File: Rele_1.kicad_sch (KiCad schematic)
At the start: 6 parts, among them J14 Rele_1, J31 Pin GND, K3 SRD-05VDC-SL-C, Q11 PMBT3904,235

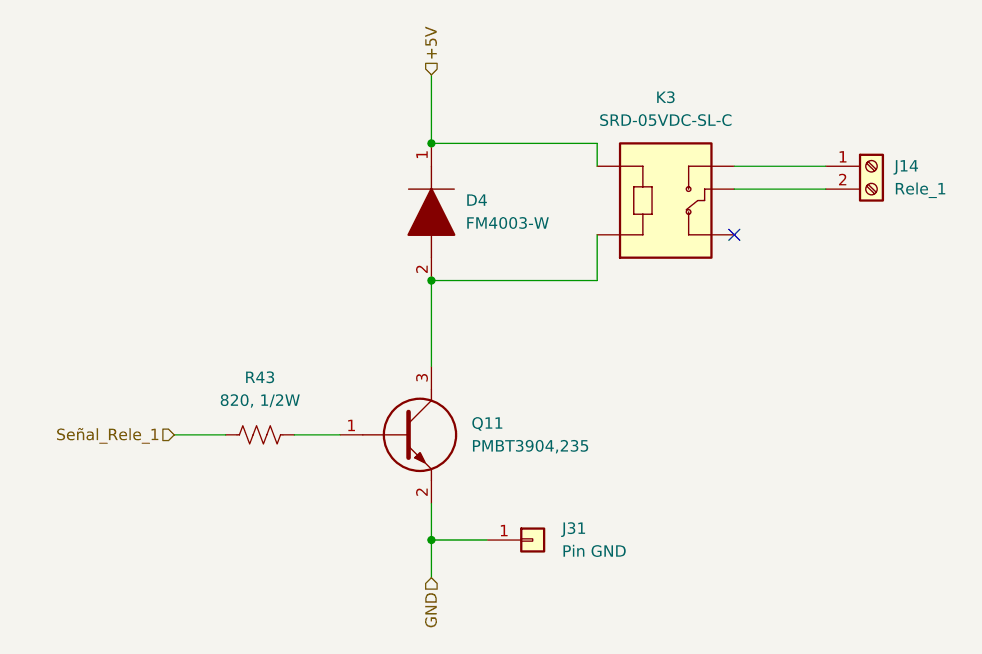
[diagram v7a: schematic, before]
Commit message: Se modificaron algunos componentes, según disponibilidad
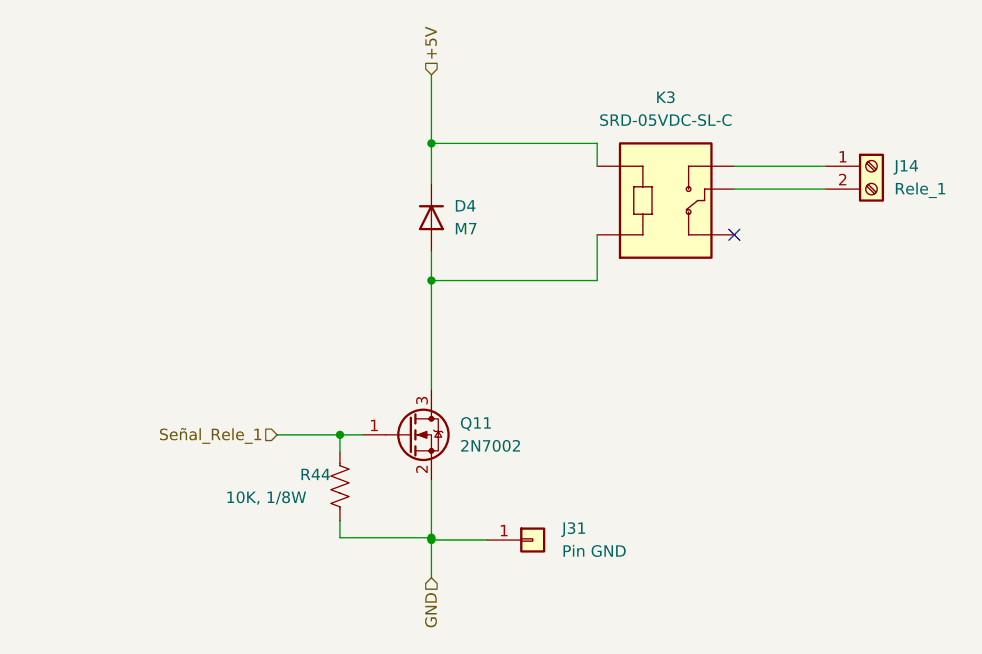
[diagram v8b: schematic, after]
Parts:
- removed D4: FM4003-W, FM4003W:DIOM5025X231N, symbol FM4003-W:FM4003-W
- removed Q11: PMBT3904,235, PMBT3904,235:SOT95P230X110-3N, symbol PMBT3904,235:PMBT3904,235
- removed R43: 820, 1/2W, Resistor_SMD:R_0805_2012Metric, symbol Device:R_US
- added D4: M7, Diode_SMD:D_SMA, symbol Device:D
- added Q11: 2N7002, Package_TO_SOT_SMD:SOT-23, symbol Transistor_FET:2N7002
- added R44: 10K, 1/8W, Resistor_SMD:R_0805_2012Metric, symbol Device:R_US
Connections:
- net +5V: now also D4.1 (K)
- net GND: now also Q11.2 (S), R44.2
- net Señal_Rele_1: now also Q11.1 (G), R44.1
- net at K3.A2: now also D4.2 (A), Q11.3 (D)
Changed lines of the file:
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@@
   (junction (at 139.7 85.09) (diameter 0) (color 0 0 0 0)
+  )
+  (junction (at 129.54 102.235) (diameter 0) (color 0 0 0 0)
+  )
+  (junction (at 139.7 113.665) (diameter 0) (color 0 0 0 0)
+  )
+  (junction (at 139.7 69.85) (diameter 0) (color 0 0 0 0)
   )
   (junction (at 139.7 113.919) (diameter 0) (color 0 0 0 0)
   )
-  (junction (at 139.7 69.85) (diameter 0) (color 0 0 0 0)
-  )
   (no_connect (at 173.355 80.01))
-  (wire (pts (xy 139.7 85.09) (xy 139.7 94.615))
+  (wire (pts (xy 139.7 85.09) (xy 139.7 97.155))
     (stroke (width 0) (type default) (color 0 0 0 0))
   )
@@
     (stroke (width 0) (type default) (color 0 0 0 0))
   )
+  (wire (pts (xy 129.54 113.665) (xy 139.7 113.665))
+    (stroke (width 0) (type default) (color 0 0 0 0))
+  )
   (wire (pts (xy 139.7 113.919) (xy 145.8722 113.919))
     (stroke (width 0) (type default) (color 0 0 0 0))
   )
-  (wire (pts (xy 124.46 102.235) (xy 129.54 102.235))
+  (wire (pts (xy 122.555 102.235) (xy 129.54 102.235))
     (stroke (width 0) (type default) (color 0 0 0 0))
   )
-  (wire (pts (xy 111.125 102.235) (xy 116.84 102.235))
+  (wire (pts (xy 129.54 111.76) (xy 129.54 113.665))
+    (stroke (width 0) (type default) (color 0 0 0 0))
+  )
+  (wire (pts (xy 139.7 69.85) (xy 139.7 74.295))
     (stroke (width 0) (type default) (color 0 0 0 0))
   )
   (wire (pts (xy 158.115 85.09) (xy 158.115 80.01))
+    (stroke (width 0) (type default) (color 0 0 0 0))
+  )
+  (wire (pts (xy 129.54 102.235) (xy 129.54 104.14))
+    (stroke (width 0) (type default) (color 0 0 0 0))
+  )
+  (wire (pts (xy 129.54 102.235) (xy 132.08 102.235))
     (stroke (width 0) (type default) (color 0 0 0 0))
   )
@@
     (stroke (width 0) (type default) (color 0 0 0 0))
   )
-  (wire (pts (xy 139.7 109.855) (xy 139.7 113.919))
+  (wire (pts (xy 139.7 113.665) (xy 139.7 113.919))
+    (stroke (width 0) (type default) (color 0 0 0 0))
+  )
+  (wire (pts (xy 139.7 107.315) (xy 139.7 113.665))
+    (stroke (width 0) (type default) (color 0 0 0 0))
+  )
+  (wire (pts (xy 139.7 81.915) (xy 139.7 85.09))
     (stroke (width 0) (type default) (color 0 0 0 0))
   )
@@
     (stroke (width 0) (type default) (color 0 0 0 0))
   )
-  (hierarchical_label "Señal_Rele_1" (shape input) (at 111.125 102.235 180)
+  (hierarchical_label "Señal_Rele_1" (shape input) (at 122.555 102.235 180)
     (effects (font (size 1.27 1.27)) (justify right))
   )
@@
     (effects (font (size 1.27 1.27)) (justify left))
   )
-  (symbol (lib_id "FM4003-W:FM4003-W") (at 139.7 69.85 270) (unit 1)
+  (symbol (lib_id "Device:D") (at 139.7 78.105 270) (unit 1)
     (in_bom yes) (on_board yes) (fields_autoplaced)
-    (property "Reference" "D4" (id 0) (at 143.51 76.1999 90)
+    (property "Reference" "D4" (id 0) (at 142.24 76.8349 90)
       (effects (font (size 1.27 1.27)) (justify left))
     )
-    (property "Value" "FM4003-W" (id 1) (at 143.51 78.7399 90)
+    (property "Value" "M7" (id 1) (at 142.24 79.3749 90)
       (effects (font (size 1.27 1.27)) (justify left))
     )
-    (property "Footprint" "FM4003W:DIOM5025X231N" (id 2) (at 139.7 81.28 0)
-      (effects (font (size 1.27 1.27)) (justify left) hide)
+    (property "Footprint" "Diode_SMD:D_SMA" (id 2) (at 139.7 78.105 0)
+      (effects (font (size 1.27 1.27)) hide)
     )
-    (property "Datasheet" "https://componentsearchengine.com/Datasheets/1/FM4003-W.pdf" (id 3) (at 137.16 81.28 0)
-      (effects (font (size 1.27 1.27)) (justify left) hide)
-    )
-    (property "Description" "Rectifiers 1A 200V GP" (id 4) (at 134.62 81.28 0)
-      (effects (font (size 1.27 1.27)) (justify left) hide)
-    )
-    (property "Height" "2.31" (id 5) (at 132.08 81.28 0)
-      (effects (font (size 1.27 1.27)) (justify left) hide)
-    )
-    (property "Manufacturer_Name" "Rectron" (id 6) (at 129.54 81.28 0)
-      (effects (font (size 1.27 1.27)) (justify left) hide)
-    )
-    (property "Manufacturer_Part_Number" "FM4003-W" (id 7) (at 127 81.28 0)
-      (effects (font (size 1.27 1.27)) (justify left) hide)
-    )
-    (property "Mouser Part Number" "583-FM4003-W" (id 8) (at 124.46 81.28 0)
-      (effects (font (size 1.27 1.27)) (justify left) hide)
-    )
-    (property "Mouser Price/Stock" "https://www.mouser.co.uk/ProductDetail/Rectron/FM4003-W/?qs=5h8Q3Z7TNRlJu6QU92Ho0w%3D%3D" (id 9) (at 121.92 81.28 0)
-      (effects (font (size 1.27 1.27)) (justify left) hide)
-    )
-    (property "Arrow Part Number" "FM4003-W" (id 10) (at 119.38 81.28 0)
-      (effects (font (size 1.27 1.27)) (justify left) hide)
-    )
-    (property "Arrow Price/Stock" "https://www.arrow.com/en/products/fm4003-w/rectron" (id 11) (at 116.84 81.28 0)
-      (effects (font (size 1.27 1.27)) (justify left) hide)
-    )
-    (property "Mouser Testing Part Number" "" (id 12) (at 114.3 81.28 0)
-      (effects (font (size 1.27 1.27)) (justify left) hide)
-    )
-    (property "Mouser Testing Price/Stock" "" (id 13) (at 111.76 81.28 0)
-      (effects (font (size 1.27 1.27)) (justify left) hide)
+    (property "Datasheet" "~" (id 3) (at 139.7 78.105 0)
+      (effects (font (size 1.27 1.27)) hide)
     )
     (pin "1")
@@
     )
     (pin "1")
+  )
+  (symbol (lib_id "Device:R_US") (at 129.54 107.95 0) (unit 1)
+    (in_bom yes) (on_board yes)
+    (property "Reference" "R44" (id 0) (at 125.095 106.68 0)
+      (effects (font (size 1.27 1.27)) (justify left))
+    )
+    (property "Value" "10K, 1/8W" (id 1) (at 116.84 109.22 0)
+      (effects (font (size 1.27 1.27)) (justify left))
+    )
+    (property "Footprint" "Resistor_SMD:R_0805_2012Metric" (id 2) (at 130.556 108.204 90)
+      (effects (font (size 1.27 1.27)) hide)
+    )
+    (property "Datasheet" "~" (id 3) (at 129.54 107.95 0)
+      (effects (font (size 1.27 1.27)) hide)
+    )
+    (pin "1")
+    (pin "2")
   )
   (symbol (lib_id "SRD-05VDC-SL-C:SRD-05VDC-SL-C") (at 165.735 74.93 0) (unit 1)
@@
     (pin "2")
   )
-  (symbol (lib_id "PMBT3904,235:PMBT3904,235") (at 129.54 102.235 0) (unit 1)
+  (symbol (lib_id "Transistor_FET:2N7002") (at 137.16 102.235 0) (unit 1)
     (in_bom yes) (on_board yes) (fields_autoplaced)
-    (property "Reference" "Q11" (id 0) (at 144.145 100.9649 0)
+    (property "Reference" "Q11" (id 0) (at 142.875 100.9649 0)
       (effects (font (size 1.27 1.27)) (justify left))
     )
-    (property "Value" "PMBT3904,235" (id 1) (at 144.145 103.5049 0)
+    (property "Value" "2N7002" (id 1) (at 142.875 103.5049 0)
       (effects (font (size 1.27 1.27)) (justify left))
     )
-    (property "Footprint" "PMBT3904,235:SOT95P230X110-3N" (id 2) (at 143.51 106.045 0)
-      (effects (font (size 1.27 1.27)) (justify left) hide)
+    (property "Footprint" "Package_TO_SOT_SMD:SOT-23" (id 2) (at 142.24 104.14 0)
+      (effects (font (size 1.27 1.27) italic) (justify left) hide)
     )
-    (property "Datasheet" "https://assets.nexperia.com/documents/data-sheet/PMBT3904.pdf" (id 3) (at 143.51 108.585 0)
-      (effects (font (size 1.27 1.27)) (justify left) hide)
-    )
-    (property "Description" "PMBT3904 - NPN switching transistor" (id 4) (at 143.51 111.125 0)
-      (effects (font (size 1.27 1.27)) (justify left) hide)
-    )
-    (property "Height" "1.1" (id 5) (at 143.51 113.665 0)
-      (effects (font (size 1.27 1.27)) (justify left) hide)
-    )
-    (property "Manufacturer_Name" "Nexperia" (id 6) (at 143.51 116.205 0)
-      (effects (font (size 1.27 1.27)) (justify left) hide)
-    )
-    (property "Manufacturer_Part_Number" "PMBT3904,235" (id 7) (at 143.51 118.745 0)
-      (effects (font (size 1.27 1.27)) (justify left) hide)
-    )
-    (property "Mouser Part Number" "771-PMBT3904235" (id 8) (at 143.51 121.285 0)
-      (effects (font (size 1.27 1.27)) (justify left) hide)
-    )
-    (property "Mouser Price/Stock" "https://www.mouser.co.uk/ProductDetail/Nexperia/PMBT3904235?qs=LOCUfHb8d9uziIfl4fmvZg%3D%3D" (id 9) (at 143.51 123.825 0)
-      (effects (font (size 1.27 1.27)) (justify left) hide)
-    )
-    (property "Arrow Part Number" "PMBT3904,235" (id 10) (at 143.51 126.365 0)
-      (effects (font (size 1.27 1.27)) (justify left) hide)
-    )
-    (property "Arrow Price/Stock" "https://www.arrow.com/en/products/pmbt3904235/nexperia?region=nac" (id 11) (at 143.51 128.905 0)
-      (effects (font (size 1.27 1.27)) (justify left) hide)
-    )
-    (property "Mouser Testing Part Number" "" (id 12) (at 143.51 131.445 0)
-      (effects (font (size 1.27 1.27)) (justify left) hide)
-    )
-    (property "Mouser Testing Price/Stock" "" (id 13) (at 143.51 133.985 0)
+    (property "Datasheet" "https://www.onsemi.com/pub/Collateral/NDS7002A-D.PDF" (id 3) (at 137.16 102.235 0)
       (effects (font (size 1.27 1.27)) (justify left) hide)
     )
@@
     (pin "3")
   )
-  (symbol (lib_id "Device:R_US") (at 120.65 102.235 90) (unit 1)
-    (in_bom yes) (on_board yes) (fields_autoplaced)
-    (property "Reference" "R43" (id 0) (at 120.65 95.885 90))
-    (property "Value" "820, 1/2W" (id 1) (at 120.65 98.425 90))
-    (property "Footprint" "Resistor_SMD:R_0805_2012Metric" (id 2) (at 120.904 101.219 90)
-      (effects (font (size 1.27 1.27)) hide)
-    )
-    (property "Datasheet" "~" (id 3) (at 120.65 102.235 0)
-      (effects (font (size 1.27 1.27)) hide)
-    )
-    (pin "1")
-    (pin "2")
-  )
 )
